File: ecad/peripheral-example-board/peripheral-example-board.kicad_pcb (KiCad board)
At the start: 2 copper layers, 105 x 70 mm, 5 parts, among them J1 Amphenol_10061913-xx0, J2 Amphenol_ACJS-MHOM, J3 Amphenol_ACJS-MHOM, J4 PJRAS2X1S01AUX, J5 NCJ9FI-H-0

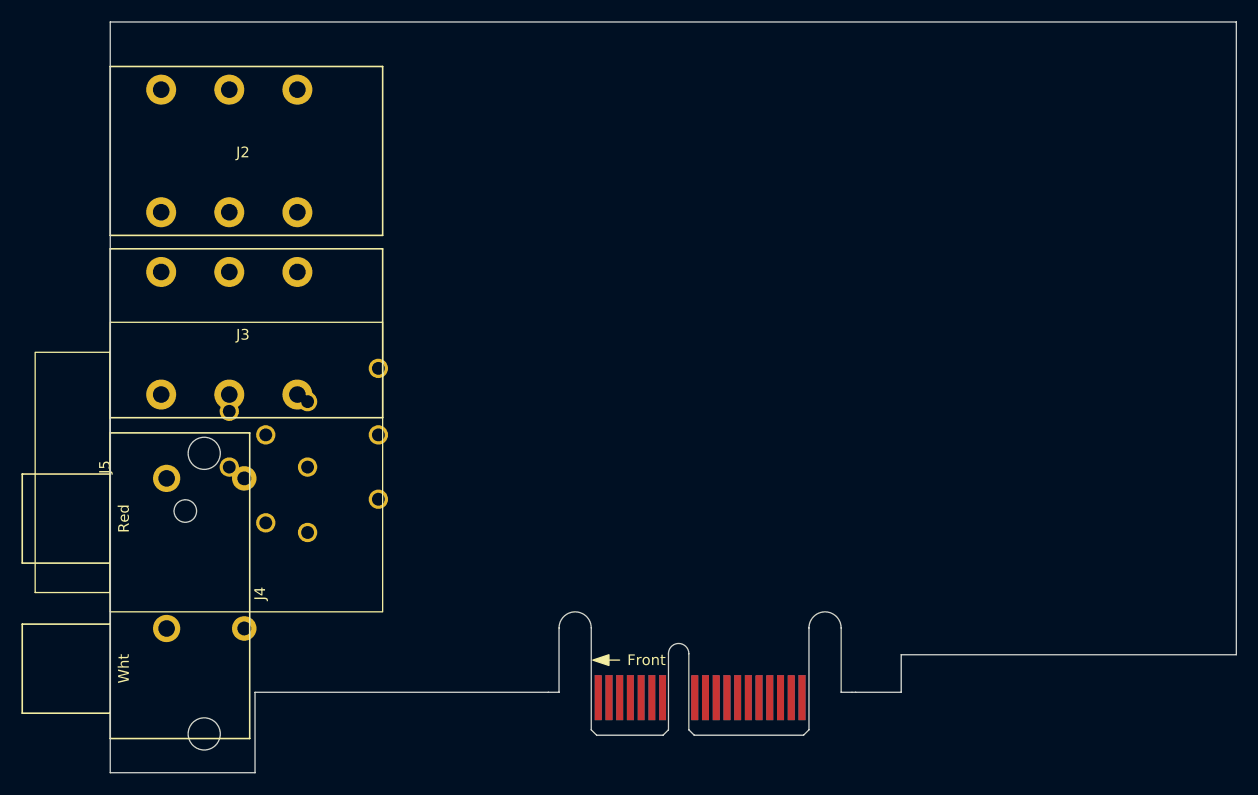
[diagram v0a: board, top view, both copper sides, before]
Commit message: Small changes and cleanup as 3dmodels are pieced together.
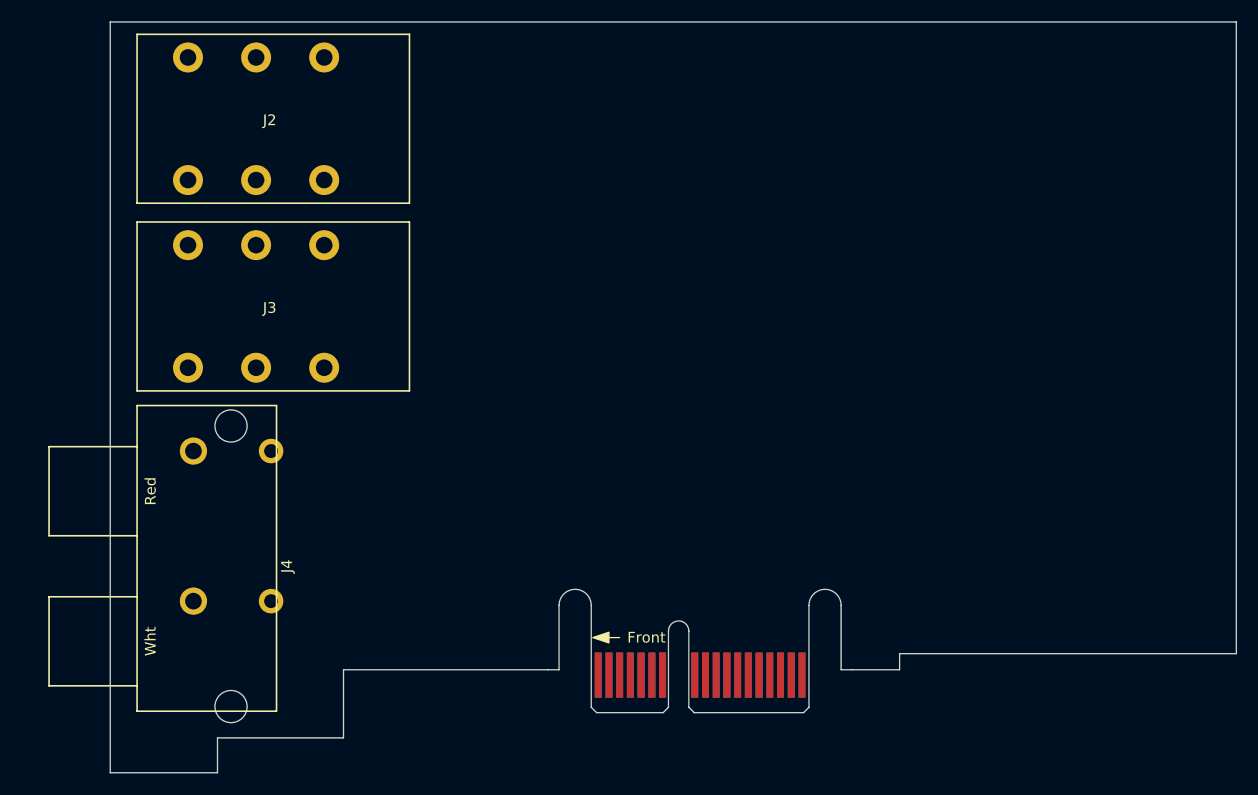
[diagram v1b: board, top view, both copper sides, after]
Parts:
- removed J5: NCJ9FI-H-0, silver-box-feetprints:Neutrik NCJ9FI-H-0
- moved J2 3.91 mm to (100.0, 78.0)
- moved J4 3.57 mm to (100.0, 121.2)
- moved J3 3.54 mm to (100.0, 95.5)
- moved J1 2.10 mm to (150.5, 134.9)
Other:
- outline, holes or cut-outs redrawn
